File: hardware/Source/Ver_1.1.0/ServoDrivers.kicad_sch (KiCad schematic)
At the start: 0 parts

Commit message: update pcb v1.1.0
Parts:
- added C29, C30: 10uF, automative_hexapod:Ceramic_Cap_0805, symbol automative_hexapod:Ceramic_Cap_0805_10uF_16V
- added C31, C32: 100nF, automative_hexapod:Ceramic_Cap_0805, symbol automative_hexapod:Ceramic_Cap_0805_100nF_50V
- added R16, R17, R18, R19, R20, R21, R22, R23, R24, R25, R26, R27, R28, R29: 10kOhm, automative_hexapod:Res_0603, symbol automative_hexapod:Res_10K_0603_1%
- added R30, R31, R32, R33, R34, R35: 220Ohm, automative_hexapod:R_Array_Convex_4x0603, symbol automative_hexapod:Res_220_4D03_5%
- added TP1, TP10, TP11, TP12, TP2, TP3, TP4, TP5, TP6, TP7, TP8, TP9: ~, automative_hexapod:SolderBridgeOpen, symbol automative_hexapod:Jumper_Open
- added U3, U4: PCA9685PW, automative_hexapod:TSSOP-28_4.4x9.7mm_P0.65mm, symbol automative_hexapod:PCA9685PW
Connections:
- new net: R29.2, U4.23 (~{OE})
- new net: R28.2, U3.23 (~{OE})
- new net +5V: C29.2, C30.2, C31.2, C32.2, TP1.2, TP10.2, TP11.2, TP12.2, TP2.2, TP3.2, TP4.2, TP5.2, TP6.2, TP7.2, TP8.2, TP9.2, U3.28 (VDD), U4.28 (VDD)
- new net A0_0: R16.2, TP1.1, U3.1 (A0)
- new net A0_1: R18.2, TP3.1, U3.2 (A1)
- new net A0_2: R20.2, TP5.1, U3.3 (A2)
- new net A0_3: R22.2, TP7.1, U3.4 (A3)
- new net A0_4: R24.2, TP9.1, U3.5 (A4)
- new net A0_5: R26.2, TP11.1, U3.24 (A5)
- new net A1_0: R17.2, TP2.1, U4.1 (A0)
- new net A1_1: R19.2, TP4.1, U4.2 (A1)
- new net A1_2: R21.2, TP6.1, U4.3 (A2)
- new net A1_3: R23.2, TP8.1, U4.4 (A3)
- new net A1_4: R25.2, TP10.1, U4.5 (A4)
- new net A1_5: R27.2, TP12.1, U4.24 (A5)
- new net CH0_0: R30.4, U3.6 (PWM0)
- new net CH0_1: R30.3, U3.7 (PWM1)
- new net CH0_2: R30.2, U3.8 (PWM2)
- new net CH0_3: R30.1, U3.9 (PWM3)
- new net CH0_4: R31.4, U3.10 (PWM4)
- new net CH0_5: R31.3, U3.11 (PWM5)
- new net CH0_6: R31.2, U3.12 (PWM6)
- new net CH0_7: R31.1, U3.13 (PWM7)
- new net CH0_8: R34.4, U3.15 (PWM8)
- new net CH1_0: R32.4, U4.6 (PWM0)
- new net CH1_1: R32.3, U4.7 (PWM1)
- new net CH1_2: R32.2, U4.8 (PWM2)
- new net CH1_3: R32.1, U4.9 (PWM3)
- new net CH1_4: R33.4, U4.10 (PWM4)
- new net CH1_5: R33.3, U4.11 (PWM5)
- new net CH1_6: R33.2, U4.12 (PWM6)
- new net CH1_7: R33.1, U4.13 (PWM7)
- new net CH1_8: R35.4, U4.15 (PWM8)
- new net GND: C29.1, C30.1, C31.1, C32.1, R16.1, R17.1, R18.1, R19.1, R20.1, R21.1, R22.1, R23.1, R24.1, R25.1, R26.1, R27.1, R28.1, R29.1, U3.14 (VSS), U3.25 (EXTCLK), U4.14 (VSS), U4.25 (EXTCLK)
- new net PCA9685_I2C_SCL: U3.26 (SCL), U4.26 (SCL)
- new net PCA9685_I2C_SDA: U3.27 (SDA), U4.27 (SDA)
- new net PCA_CH0_0: R30.5
- new net PCA_CH0_1: R30.6
- new net PCA_CH0_2: R30.7
- new net PCA_CH0_3: R30.8
- new net PCA_CH0_4: R31.5
- new net PCA_CH0_5: R31.6
- new net PCA_CH0_6: R31.7
- new net PCA_CH0_7: R31.8
- new net PCA_CH0_8: R34.5
- new net PCA_CH1_0: R32.5
- new net PCA_CH1_1: R32.6
- new net PCA_CH1_2: R32.7
- new net PCA_CH1_3: R32.8
- new net PCA_CH1_4: R33.5
- new net PCA_CH1_5: R33.6
- new net PCA_CH1_6: R33.7
- new net PCA_CH1_7: R33.8
- new net PCA_CH1_8: R35.5
- no-connect marks 0 -> 26
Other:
- note added: "Servo Driver - Channel 0"
- note added: "Servo Driver - Channel 1"
- title: (none) -> SERVO DRIVERS

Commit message: update pcb and schematic
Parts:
- removed C29, C30: 10uF, automative_hexapod:Ceramic_Cap_0805, symbol automative_hexapod:Ceramic_Cap_0805_10uF_16V
- removed C31, C32: 100nF, automative_hexapod:Ceramic_Cap_0805, symbol automative_hexapod:Ceramic_Cap_0805_100nF_50V
- added C23, C24: 10uF, automative_hexapod:Ceramic_Cap_0603, symbol automative_hexapod:Ceramic_Cap_0603_10uF_25V
- added C25, C26: 100nF, automative_hexapod:Ceramic_Cap_0603, symbol automative_hexapod:Ceramic_Cap_0603_100nF_50V
- renumbered R16 to R18, R17 to R19, R18 to R20, R19 to R21, R20 to R22, R21 to R23, R22 to R24, R23 to R25, R24 to R26, R25 to R27, R26 to R28, R27 to R29, R28 to R30, R29 to R31, R30 to R32, R31 to R33, R32 to R34, R33 to R35, R34 to R36, R35 to R37
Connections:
- net +5V: no longer U3.28 (VDD), U4.28 (VDD)
- net GND: now also C23.1, C24.1, C25.1, C26.1
- net PCA9685_I2C_SCL renamed BBAI_I2C_SCL
- net PCA9685_I2C_SDA renamed BBAI_I2C_SDA
- new net +3.3V: C23.2, C24.2, C25.2, C26.2, U3.28 (VDD), U4.28 (VDD)

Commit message: Update PCB
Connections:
- net +5V is gone; now on net +3.3V: TP1.2, TP10.2, TP11.2, TP12.2, TP2.2, TP3.2, TP4.2, TP5.2, TP6.2, TP7.2, TP8.2, TP9.2

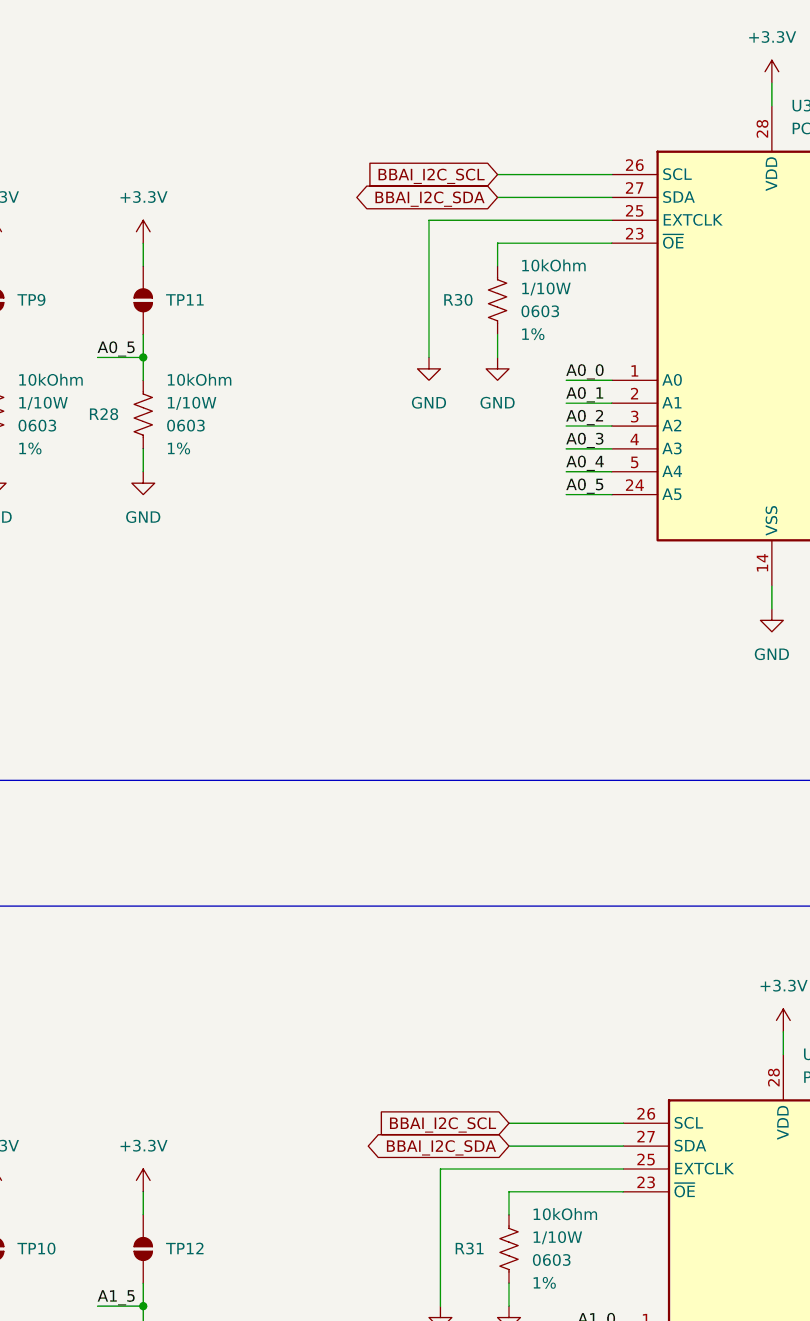
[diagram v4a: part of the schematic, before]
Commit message: Generate PDF Schematic Ver1.1.0 and add README.md
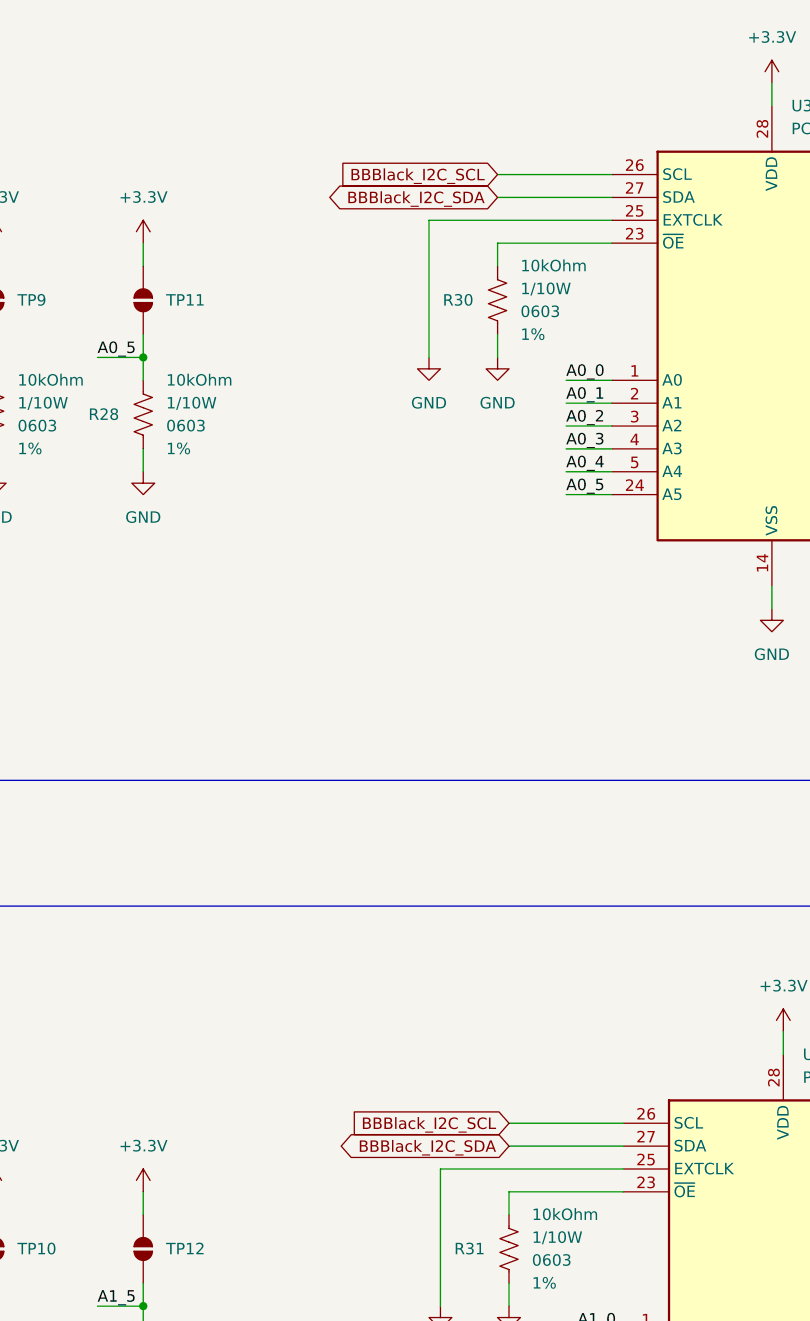
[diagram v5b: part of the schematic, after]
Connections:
- net BBAI_I2C_SCL renamed BBBlack_I2C_SCL
- net BBAI_I2C_SDA renamed BBBlack_I2C_SDA
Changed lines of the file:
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@@
 		)
 	)
-	(global_label "BBAI_I2C_SDA"
+	(global_label "BBBlack_I2C_SDA"
 		(shape bidirectional)
 		(at 162.56 60.96 180)
@@
 		)
 	)
-	(global_label "BBAI_I2C_SCL"
+	(global_label "BBBlack_I2C_SCL"
 		(shape input)
 		(at 163.83 163.83 180)
@@
 		)
 	)
-	(global_label "BBAI_I2C_SDA"
+	(global_label "BBBlack_I2C_SDA"
 		(shape bidirectional)
 		(at 163.83 166.37 180)
@@
 		)
 	)
-	(global_label "BBAI_I2C_SCL"
+	(global_label "BBBlack_I2C_SCL"
 		(shape input)
 		(at 162.56 58.42 180)
